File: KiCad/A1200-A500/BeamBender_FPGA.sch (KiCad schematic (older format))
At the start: 29 parts, among them J6 Conn_02x06_Odd_Even, U2 GW1NR-UV9LQ144P, U5 AK5720VT, X3 5.0x3.2mm

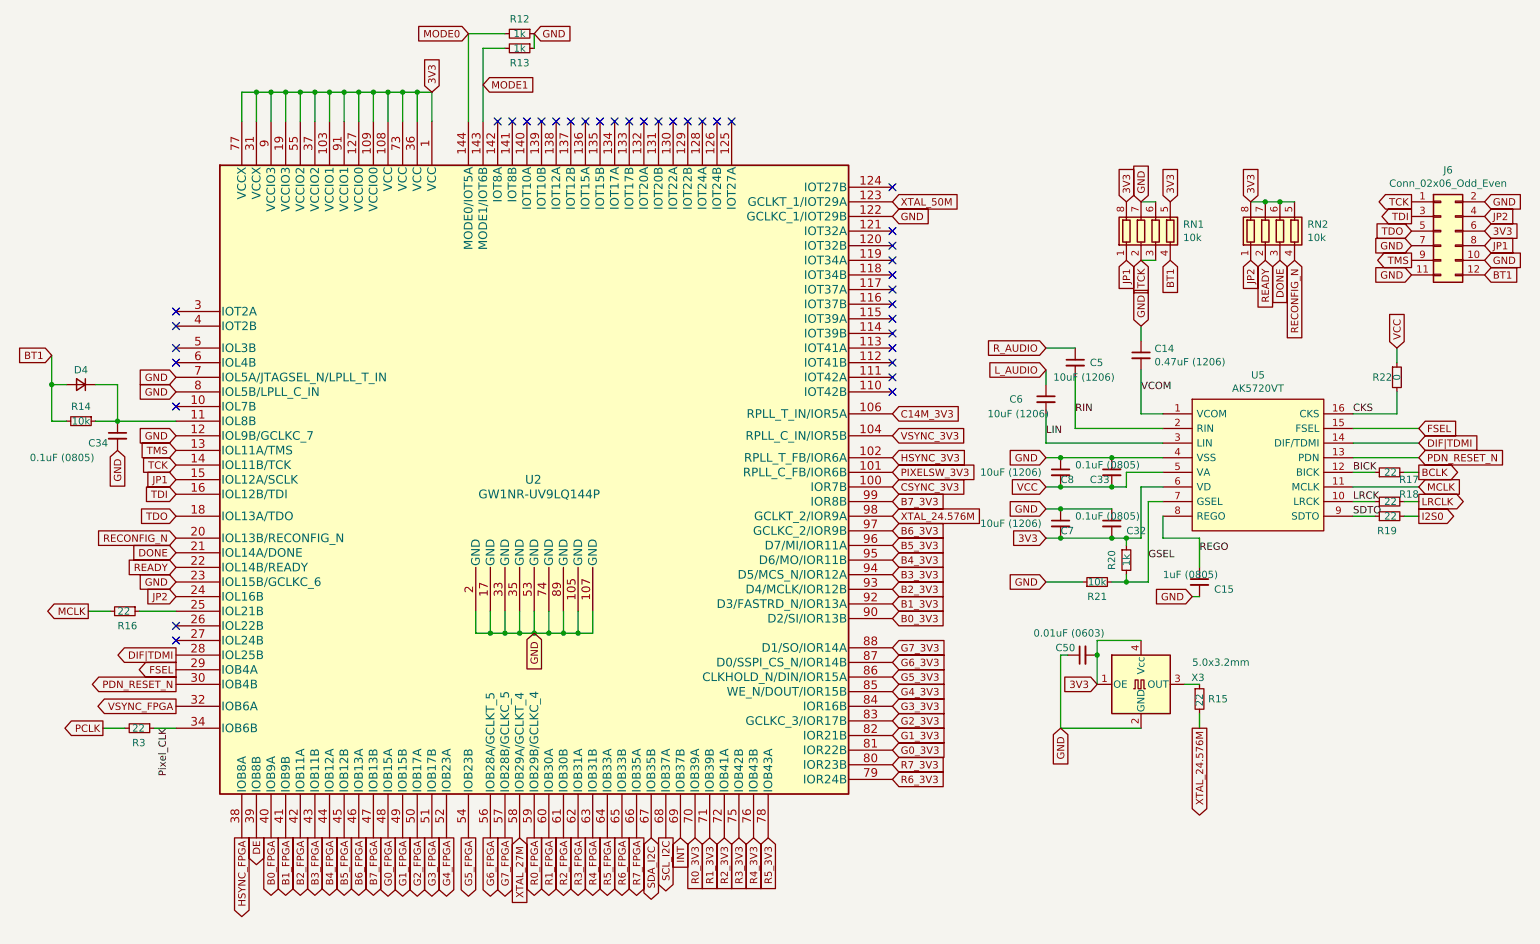
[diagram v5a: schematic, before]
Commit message: Fixed enumeration/order of all resistors on board and their reference placement on silkscreen
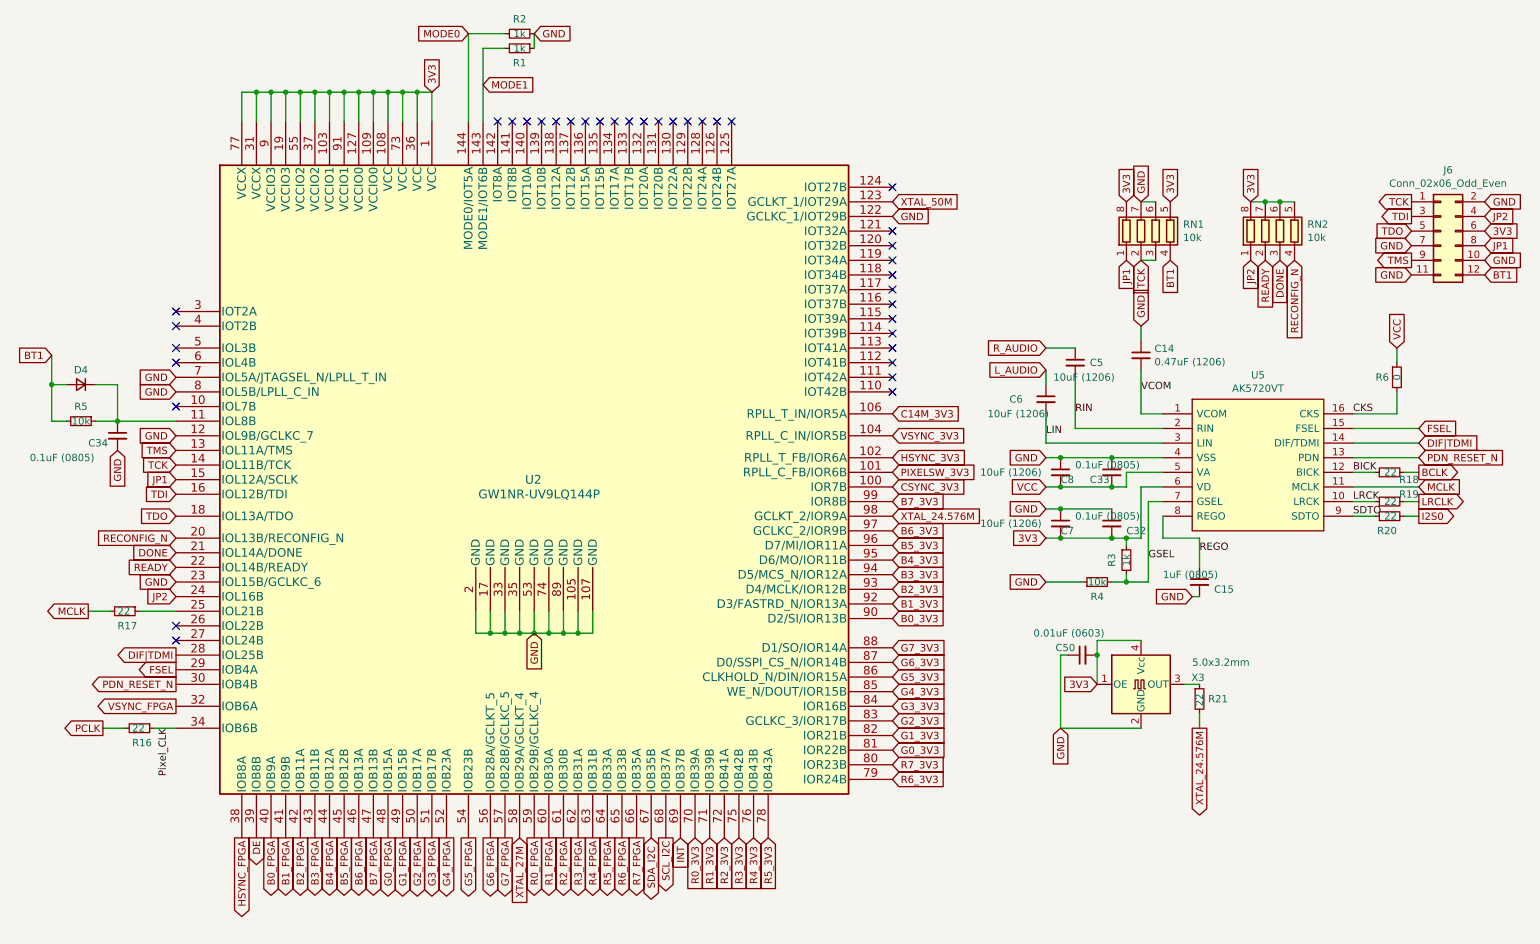
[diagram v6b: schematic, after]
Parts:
- renumbered R13 to R1, R3 to R16, R16 to R17, R17 to R18, R18 to R19, R12 to R2, R19 to R20, R15 to R21, R20 to R3, R21 to R4, R14 to R5, R22 to R6
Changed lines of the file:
@@
 P 1350 5400
 AR Path="/65968AC9" Ref="R?"  Part="1"
-AR Path="/6541C824/65968AC9" Ref="R3"  Part="1"
-F 0 "R3" V 1450 5350 50  0000 L CNN
+AR Path="/6541C824/65968AC9" Ref="R16"  Part="1"
+F 0 "R16" V 1450 5350 50  0000 L CNN
 F 1 "22" V 1350 5350 50  0000 L CNN
 F 2 "Resistor_SMD:R_0603_1608Metric_Pad0.98x0.95mm_HandSolder" H 1350 5400 50  0001 C CNN
@@
 GND
 $Comp
-L Device:R_Small R13
+L Device:R_Small R1
 U 1 1 661C34A6
 P 3950 750
-F 0 "R13" V 4050 750 50  0000 C CNN
+F 0 "R1" V 4050 750 50  0000 C CNN
 F 1 "1k" V 3950 750 50  0000 C CNN
 F 2 "Resistor_SMD:R_0805_2012Metric_Pad1.20x1.40mm_HandSolder" H 3950 750 50  0001 C CNN
@@
 $EndComp
 $Comp
-L Device:R_Small R12
+L Device:R_Small R2
 U 1 1 661D4C0B
 P 3950 650
-F 0 "R12" V 3850 650 50  0000 C CNN
+F 0 "R2" V 3850 650 50  0000 C CNN
 F 1 "1k" V 3950 650 50  0000 C CNN
 F 2 "Resistor_SMD:R_0805_2012Metric_Pad1.20x1.40mm_HandSolder" H 3950 650 50  0001 C CNN
@@
 $EndComp
 $Comp
-L Device:R_Small R14
+L Device:R_Small R5
 U 1 1 6651553B
 P 950 3300
-F 0 "R14" V 850 3300 50  0000 C CNN
+F 0 "R5" V 850 3300 50  0000 C CNN
 F 1 "10k" V 950 3300 50  0000 C CNN
 F 2 "Resistor_SMD:R_0805_2012Metric_Pad1.20x1.40mm_HandSolder" H 950 3300 50  0001 C CNN
@@
 	7900 4800 7900 4900
 $Comp
-L Device:R_Small R15
+L Device:R_Small R21
 U 1 1 665DD143
 P 8600 5200
-F 0 "R15" H 8659 5200 50  0000 L CNN
+F 0 "R21" H 8659 5200 50  0000 L CNN
 F 1 "22" V 8600 5150 50  0000 L CNN
 F 2 "Resistor_SMD:R_0603_1608Metric_Pad0.98x0.95mm_HandSolder" H 8600 5200 50  0001 C CNN
@@
 P 1250 4600
 AR Path="/666738D2" Ref="R?"  Part="1"
-AR Path="/6541C824/666738D2" Ref="R16"  Part="1"
-F 0 "R16" V 1350 4550 50  0000 L CNN
+AR Path="/6541C824/666738D2" Ref="R17"  Part="1"
+F 0 "R17" V 1350 4550 50  0000 L CNN
 F 1 "22" V 1250 4550 50  0000 L CNN
 F 2 "Resistor_SMD:R_0603_1608Metric_Pad0.98x0.95mm_HandSolder" H 1250 4600 50  0001 C CNN
@@
 	1350 4600 1600 4600
 $Comp
-L Device:R_Small R17
+L Device:R_Small R18
 U 1 1 666AAB38
 P 9900 3650
-F 0 "R17" V 9850 3450 50  0000 L CNN
+F 0 "R18" V 9850 3450 50  0000 L CNN
 F 1 "22" V 9900 3600 50  0000 L CNN
 F 2 "Resistor_SMD:R_0603_1608Metric_Pad0.98x0.95mm_HandSolder" H 9900 3650 50  0001 C CNN
@@
 $EndComp
 $Comp
-L Device:R_Small R18
+L Device:R_Small R19
 U 1 1 666AD788
 P 9900 3850
-F 0 "R18" V 9950 3650 50  0000 L CNN
+F 0 "R19" V 9950 3650 50  0000 L CNN
 F 1 "22" V 9900 3800 50  0000 L CNN
 F 2 "Resistor_SMD:R_0603_1608Metric_Pad0.98x0.95mm_HandSolder" H 9900 3850 50  0001 C CNN
@@
 $EndComp
 $Comp
-L Device:R_Small R19
+L Device:R_Small R20
 U 1 1 666AF72B
 P 9900 3950
-F 0 "R19" V 9800 3900 50  0000 L CNN
+F 0 "R20" V 9800 3900 50  0000 L CNN
 F 1 "22" V 9900 3900 50  0000 L CNN
 F 2 "Resistor_SMD:R_0603_1608Metric_Pad0.98x0.95mm_HandSolder" H 9900 3950 50  0001 C CNN
@@
 	8350 3850 8250 3850
 $Comp
-L Device:R_Small R20
+L Device:R_Small R3
 U 1 1 668DB86F
 P 8100 4250
-F 0 "R20" V 8000 4250 50  0000 C CNN
+F 0 "R3" V 8000 4250 50  0000 C CNN
 F 1 "1k" V 8100 4250 50  0000 C CNN
 F 2 "Resistor_SMD:R_0805_2012Metric_Pad1.20x1.40mm_HandSolder" H 8100 4250 50  0001 C CNN
@@
 CKS
 $Comp
-L Device:R_Small R22
+L Device:R_Small R6
 U 1 1 66968A2E
 P 9950 3000
-F 0 "R22" H 9850 3000 50  0000 C CNN
+F 0 "R6" H 9850 3000 50  0000 C CNN
 F 1 "0" V 9950 3000 50  0000 C CNN
 F 2 "Resistor_SMD:R_0805_2012Metric_Pad1.20x1.40mm_HandSolder" H 9950 3000 50  0001 C CNN
@@
 FSEL
 $Comp
-L Device:R_Small R21
+L Device:R_Small R4
 U 1 1 66A36561
 P 7900 4400
-F 0 "R21" V 7800 4400 50  0000 C CNN
+F 0 "R4" V 7800 4400 50  0000 C CNN
 F 1 "10k" V 7900 4400 50  0000 C CNN
 F 2 "Resistor_SMD:R_0805_2012Metric_Pad1.20x1.40mm_HandSolder" H 7900 4400 50  0001 C CNN

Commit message: Fixed ordering of L1-L4, changed R14-R21 to 33 Ohms, and swapped X2 and X3 reference
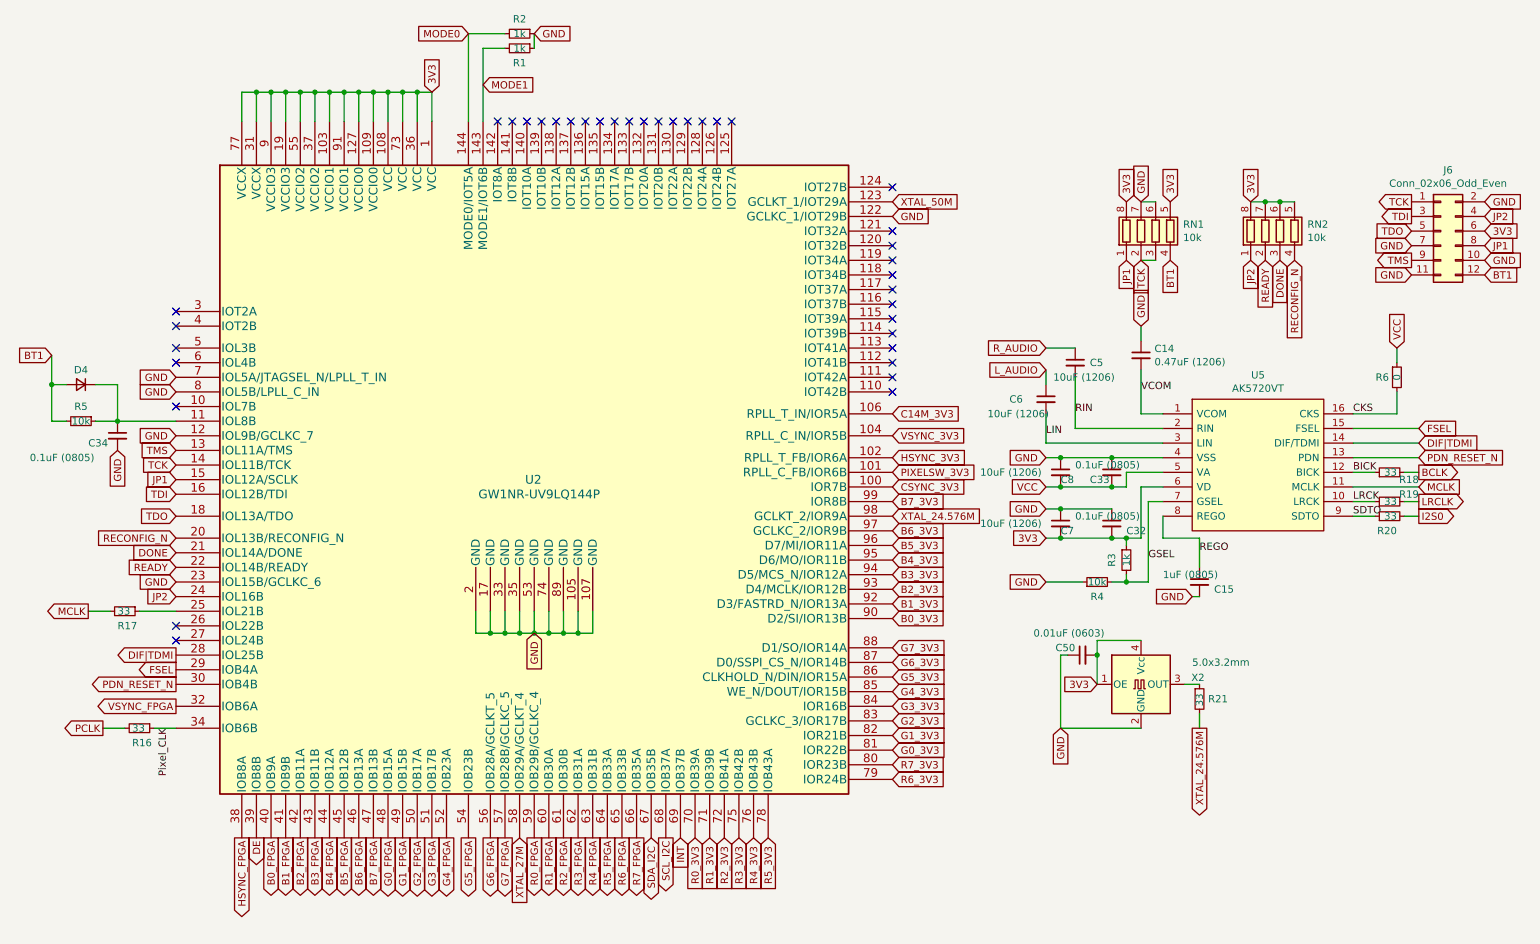
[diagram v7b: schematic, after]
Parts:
- R16, R17, R18, R19, R20, R21: value 22 -> 33
- renumbered X3 to X2
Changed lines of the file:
@@
 AR Path="/6541C824/65968AC9" Ref="R16"  Part="1"
 F 0 "R16" V 1450 5350 50  0000 L CNN
-F 1 "22" V 1350 5350 50  0000 L CNN
+F 1 "33" V 1350 5350 50  0000 L CNN
 F 2 "Resistor_SMD:R_0603_1608Metric_Pad0.98x0.95mm_HandSolder" H 1350 5400 50  0001 C CNN
 F 3 "~" H 1350 5400 50  0001 C CNN
@@
 P 8600 5200
 F 0 "R21" H 8659 5200 50  0000 L CNN
-F 1 "22" V 8600 5150 50  0000 L CNN
+F 1 "33" V 8600 5150 50  0000 L CNN
 F 2 "Resistor_SMD:R_0603_1608Metric_Pad0.98x0.95mm_HandSolder" H 8600 5200 50  0001 C CNN
 F 3 "~" H 8600 5200 50  0001 C CNN
@@
 	7650 4900 7700 4900
 $Comp
-L Oscillator:SG-8002LB X3
+L Oscillator:SG-8002LB X2
 U 1 1 665EF5A4
 P 8200 5100
-F 0 "X3" H 8544 5146 50  0000 L CNN
+F 0 "X2" H 8544 5146 50  0000 L CNN
 F 1 "5.0x3.2mm" H 8550 5250 50  0000 L CNN
 F 2 "Oscillator:Oscillator_SMD_TXC_7C-4Pin_5.0x3.2mm_HandSoldering" H 8900 4750 50  0001 C CNN
@@
 AR Path="/6541C824/666738D2" Ref="R17"  Part="1"
 F 0 "R17" V 1350 4550 50  0000 L CNN
-F 1 "22" V 1250 4550 50  0000 L CNN
+F 1 "33" V 1250 4550 50  0000 L CNN
 F 2 "Resistor_SMD:R_0603_1608Metric_Pad0.98x0.95mm_HandSolder" H 1250 4600 50  0001 C CNN
 F 3 "~" H 1250 4600 50  0001 C CNN
@@
 P 9900 3650
 F 0 "R18" V 9850 3450 50  0000 L CNN
-F 1 "22" V 9900 3600 50  0000 L CNN
+F 1 "33" V 9900 3600 50  0000 L CNN
 F 2 "Resistor_SMD:R_0603_1608Metric_Pad0.98x0.95mm_HandSolder" H 9900 3650 50  0001 C CNN
 F 3 "~" H 9900 3650 50  0001 C CNN
@@
 P 9900 3850
 F 0 "R19" V 9950 3650 50  0000 L CNN
-F 1 "22" V 9900 3800 50  0000 L CNN
+F 1 "33" V 9900 3800 50  0000 L CNN
 F 2 "Resistor_SMD:R_0603_1608Metric_Pad0.98x0.95mm_HandSolder" H 9900 3850 50  0001 C CNN
 F 3 "~" H 9900 3850 50  0001 C CNN
@@
 P 9900 3950
 F 0 "R20" V 9800 3900 50  0000 L CNN
-F 1 "22" V 9900 3900 50  0000 L CNN
+F 1 "33" V 9900 3900 50  0000 L CNN
 F 2 "Resistor_SMD:R_0603_1608Metric_Pad0.98x0.95mm_HandSolder" H 9900 3950 50  0001 C CNN
 F 3 "~" H 9900 3950 50  0001 C CNN
